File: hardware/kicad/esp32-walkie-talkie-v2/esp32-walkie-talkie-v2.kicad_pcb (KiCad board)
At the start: 2 copper layers, 68.6 x 53.3 mm, 22 parts, among them J1 inmp441 left, J2 inmp441 right, J3 ST7789, J4 extend, J5 POWER_IN_5V, J6 MAX98357, J7 POWER_IN_5V, P1 Power, P2 Analog, P3 Digital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

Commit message: update silk, export gerber
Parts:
- added kibuzzard-62A4A288: G***, kibuzzard-62A4A288, F.Cu at (130.0, 88.3)
- added kibuzzard-62A4A2A0: G***, kibuzzard-62A4A2A0, F.Cu at (122.9, 106.6)
- added kibuzzard-62A534F6: G***, kibuzzard-62A534F6, F.Cu at (171.7, 82.2)
- added kibuzzard-62A53545: G***, kibuzzard-62A53545, F.Cu at (114.3, 106.8)
- added kibuzzard-62A53555: G***, kibuzzard-62A53555, F.Cu at (130.0, 90.6)
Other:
- board text added: "LRC"
- board text removed: "LRCLK"

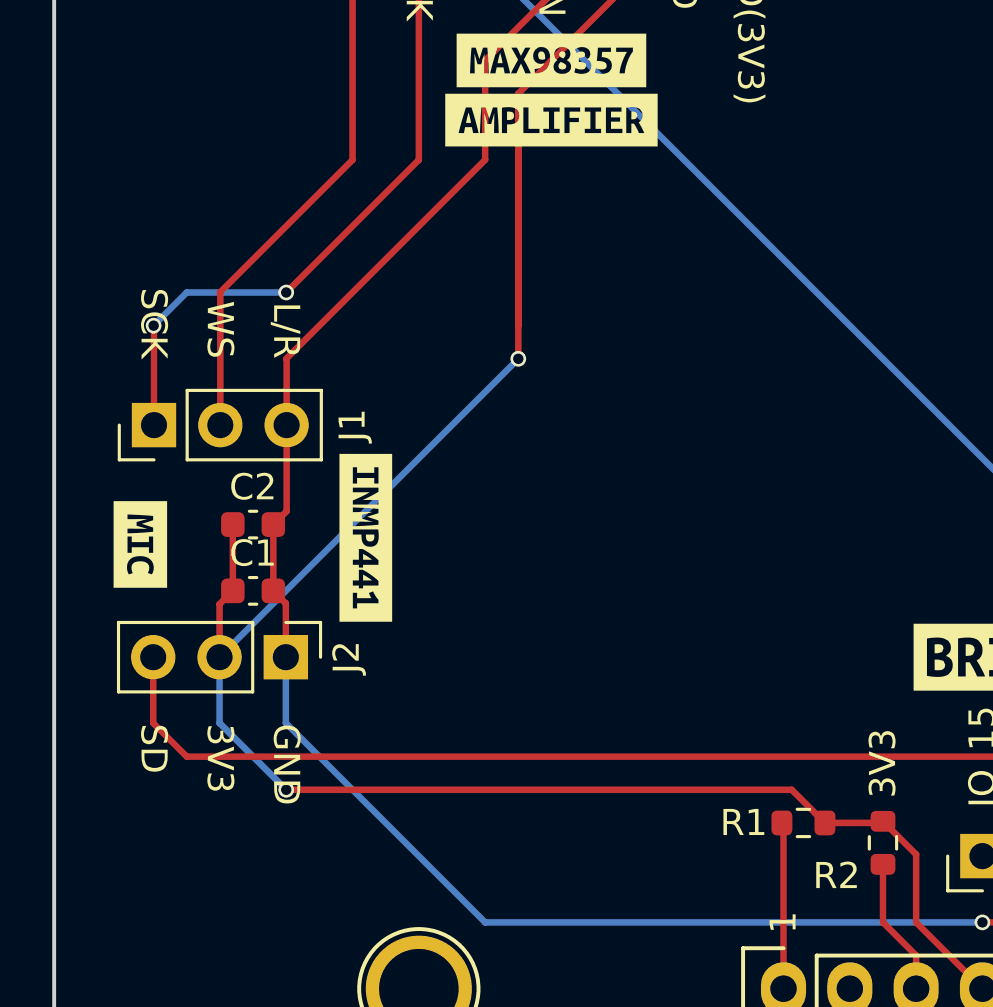
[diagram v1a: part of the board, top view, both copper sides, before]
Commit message: add option capacitor
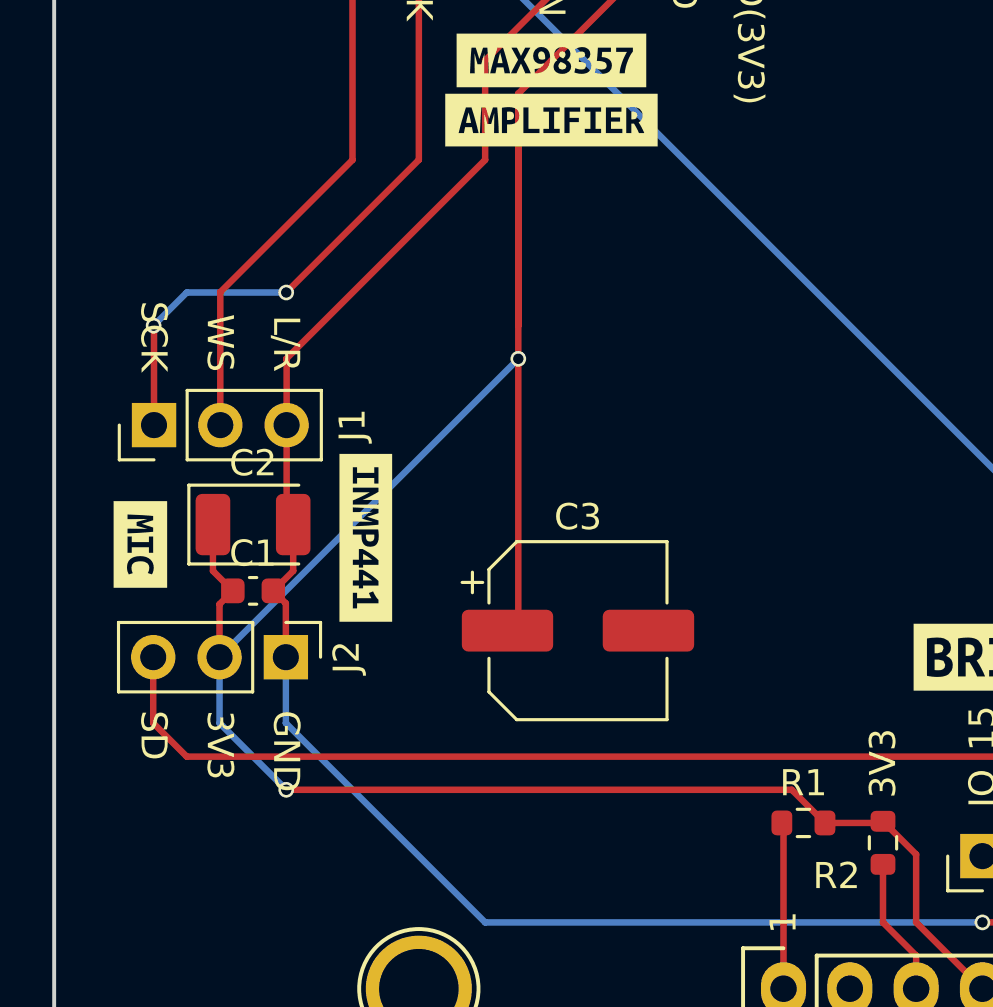
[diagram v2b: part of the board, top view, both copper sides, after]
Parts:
- added C3: 47uF, Capacitor_SMD:CP_Elec_6.3x5.8, F.Cu at (131.1, 110.1)
- C2: value 1uF -> 10uF; footprint Capacitor_SMD:C_0603_1608Metric -> Capacitor_Tantalum_SMD:CP_EIA-3528-12_Kemet-T
- J7: value POWER_IN_5V -> Transimit switch
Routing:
- net ESPDUINO_3.3V: track 142.5 -> 153.4 mm

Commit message: add rect capacitor option
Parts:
- added C4: 47uF, Capacitor_THT:C_Rect_L7.0mm_W2.0mm_P5.00mm, F.Cu at (128.6, 118.5)
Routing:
- net ESPDUINO_3.3V: track 153.4 -> 167.0 mm, vias 3 -> 4
- net GND: vias 1 -> 18
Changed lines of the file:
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@@
       ) (layer "F.SilkS") (width 0) (fill solid))
+  )
+  (footprint "Capacitor_THT:C_Rect_L7.0mm_W2.0mm_P5.00mm" (layer "F.Cu")
+    (at 128.564 118.491)
+    (descr "C, Rect series, Radial, pin pitch=5.00mm, , length*width=7*2mm^2, Capacitor")
+    (tags "C Rect series Radial pin pitch 5.00mm  length 7mm width 2mm Capacitor")
+    (property "Sheetfile" "esp32-walkie-talkie-v2.kicad_sch")
+    (property "Sheetname" "")
+    (attr through_hole)
+    (fp_text reference "C4" (at 2.5 -2.25) (layer "F.SilkS")
+      (effects (font (size 1 1) (thickness 0.15)))
+    )
+    (fp_text value "47uF" (at 2.5 2.25) (layer "F.Fab")
+      (effects (font (size 1 1) (thickness 0.15)))
+    )
+    (fp_text user "${REFERENCE}" (at 2.5 0) (layer "F.Fab")
+      (effects (font (size 1 1) (thickness 0.15)))
+    )
+    (fp_line (start -1.12 1.12) (end 6.12 1.12) (layer "F.SilkS") (width 0.12))
+    (fp_line (start 6.12 -1.12) (end 6.12 1.12) (layer "F.SilkS") (width 0.12))
+    (fp_line (start -1.12 -1.12) (end -1.12 1.12) (layer "F.SilkS") (width 0.12))
+    (fp_line (start -1.12 -1.12) (end 6.12 -1.12) (layer "F.SilkS") (width 0.12))
+    (fp_line (start 6.25 1.25) (end 6.25 -1.25) (layer "F.CrtYd") (width 0.05))
+    (fp_line (start 6.25 -1.25) (end -1.25 -1.25) (layer "F.CrtYd") (width 0.05))
+    (fp_line (start -1.25 -1.25) (end -1.25 1.25) (layer "F.CrtYd") (width 0.05))
+    (fp_line (start -1.25 1.25) (end 6.25 1.25) (layer "F.CrtYd") (width 0.05))
+    (fp_line (start 6 -1) (end -1 -1) (layer "F.Fab") (width 0.1))
+    (fp_line (start 6 1) (end 6 -1) (layer "F.Fab") (width 0.1))
+    (fp_line (start -1 1) (end 6 1) (layer "F.Fab") (width 0.1))
+    (fp_line (start -1 -1) (end -1 1) (layer "F.Fab") (width 0.1))
+    (pad "1" thru_hole circle (at 0 0) (size 1.6 1.6) (drill 0.8) (layers *.Cu *.Mask)
+      (net 34 "ESPDUINO_3.3V") (pintype "passive"))
+    (pad "2" thru_hole circle (at 5 0) (size 1.6 1.6) (drill 0.8) (layers *.Cu *.Mask)
+      (net 3 "GND") (pintype "passive"))
+    (model "${KICAD6_3DMODEL_DIR}/Capacitor_THT.3dshapes/C_Rect_L7.0mm_W2.0mm_P5.00mm.wrl"
+      (offset (xyz 0 0 0))
+      (scale (xyz 1 1 1))
+      (rotate (xyz 0 0 0))
+    )
   )
   (footprint "Capacitor_SMD:C_0603_1608Metric" (layer "F.Cu")
@@
   (segment (start 120.1555 107.8225) (end 119.393 108.585) (width 0.25) (layer "F.Cu") (net 3))
   (segment (start 119.903 99.71) (end 119.903 102.235) (width 0.25) (layer "F.Cu") (net 3))
+  (via (at 168.656 80.645) (size 0.6) (drill 0.4) (layers "F.Cu" "B.Cu") (free) (net 3))
+  (via (at 168.148 98.171) (size 0.6) (drill 0.4) (layers "F.Cu" "B.Cu") (free) (net 3))
+  (via (at 168.656 83.439) (size 0.6) (drill 0.4) (layers "F.Cu" "B.Cu") (free) (net 3))
+  (via (at 132.08 123.571) (size 0.6) (drill 0.4) (layers "F.Cu" "B.Cu") (free) (net 3))
+  (via (at 138.938 112.141) (size 0.6) (drill 0.4) (layers "F.Cu" "B.Cu") (free) (net 3))
   (via (at 146.558 121.285) (size 0.6) (drill 0.4) (layers "F.Cu" "B.Cu") (net 3))
+  (via (at 163.068 112.395) (size 0.6) (drill 0.4) (layers "F.Cu" "B.Cu") (free) (net 3))
+  (via (at 164.338 91.059) (size 0.6) (drill 0.4) (layers "F.Cu" "B.Cu") (free) (net 3))
+  (via (at 155.956 92.329) (size 0.6) (drill 0.4) (layers "F.Cu" "B.Cu") (free) (net 3))
+  (via (at 174.498 107.823) (size 0.6) (drill 0.4) (layers "F.Cu" "B.Cu") (free) (net 3))
+  (via (at 144.78 86.995) (size 0.6) (drill 0.4) (layers "F.Cu" "B.Cu") (free) (net 3))
+  (via (at 119.126 91.567) (size 0.6) (drill 0.4) (layers "F.Cu" "B.Cu") (free) (net 3))
+  (via (at 169.418 120.523) (size 0.6) (drill 0.4) (layers "F.Cu" "B.Cu") (free) (net 3))
+  (via (at 114.808 118.745) (size 0.6) (drill 0.4) (layers "F.Cu" "B.Cu") (free) (net 3))
+  (via (at 125.476 107.061) (size 0.6) (drill 0.4) (layers "F.Cu" "B.Cu") (free) (net 3))
+  (via (at 119.126 80.645) (size 0.6) (drill 0.4) (layers "F.Cu" "B.Cu") (free) (net 3))
+  (via (at 125.222 99.695) (size 0.6) (drill 0.4) (layers "F.Cu" "B.Cu") (free) (net 3))
+  (via (at 145.034 78.867) (size 0.6) (drill 0.4) (layers "F.Cu" "B.Cu") (free) (net 3))
   (segment (start 168.148 114.935) (end 170.688 114.935) (width 0.25) (layer "B.Cu") (net 3))
   (segment (start 155.448 121.285) (end 161.798 121.285) (width 0.25) (layer "B.Cu") (net 3))
@@
   (segment (start 117.0805 106.045) (end 117.0805 107.8225) (width 0.25) (layer "F.Cu") (net 34))
   (segment (start 142.685 117.475) (end 142.748 117.412) (width 0.25) (layer "F.Cu") (net 34))
+  (segment (start 124.714 112.141) (end 126.746 110.109) (width 0.25) (layer "F.Cu") (net 34))
   (segment (start 128.778 99.695) (end 128.778 109.695) (width 0.25) (layer "F.Cu") (net 34))
+  (segment (start 126.746 110.109) (end 128.364 110.109) (width 0.25) (layer "F.Cu") (net 34))
   (segment (start 128.778 109.695) (end 128.364 110.109) (width 0.25) (layer "F.Cu") (net 34))
   (segment (start 117.0805 107.8225) (end 117.843 108.585) (width 0.25) (layer "F.Cu") (net 34))
@@
   (segment (start 139.255 116.205) (end 119.888 116.205) (width 0.25) (layer "F.Cu") (net 34))
   (via (at 119.888 116.205) (size 0.6) (drill 0.4) (layers "F.Cu" "B.Cu") (net 34))
+  (via (at 124.714 112.141) (size 0.6) (drill 0.4) (layers "F.Cu" "B.Cu") (net 34))
   (via (at 168.148 94.615) (size 0.6) (drill 0.4) (layers "F.Cu" "B.Cu") (net 34))
   (via (at 128.778 99.695) (size 0.6) (drill 0.4) (layers "F.Cu" "B.Cu") (net 34))
@@
   (segment (start 117.333 113.65) (end 117.333 111.125) (width 0.25) (layer "B.Cu") (net 34))
   (segment (start 123.698 104.76) (end 123.713 104.76) (width 0.25) (layer "B.Cu") (net 34))
+  (segment (start 124.968 116.967) (end 124.714 116.713) (width 0.25) (layer "B.Cu") (net 34))
   (segment (start 174.498 90.85) (end 174.498 83.185) (width 0.25) (layer "B.Cu") (net 34))
   (segment (start 123.698 104.76) (end 117.333 111.125) (width 0.25) (layer "B.Cu") (net 34))
+  (segment (start 126.492 118.491) (end 124.968 116.967) (width 0.25) (layer "B.Cu") (net 34))
+  (segment (start 124.714 116.713) (end 124.714 112.141) (width 0.25) (layer "B.Cu") (net 34))
   (segment (start 123.713 104.76) (end 128.778 99.695) (width 0.25) (layer "B.Cu") (net 34))
+  (segment (start 128.564 118.491) (end 126.492 118.491) (width 0.25) (layer "B.Cu") (net 34))
   (segment (start 168.168 94.635) (end 168.148 94.615) (width 0.25) (layer "B.Cu") (net 34))
   (segment (start 170.713 94.635) (end 174.498 90.85) (width 0.25) (layer "B.Cu") (net 34))

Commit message: add text, new copper fill
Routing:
- net GND: track 105.4 -> 0.00 mm, vias 18 -> 17
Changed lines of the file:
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@@
     (fp_line (start -1.05 -1.4) (end -1.75 -0.7) (layer "F.Fab") (width 0.1))
     (fp_line (start 1.75 1.4) (end 1.75 -1.4) (layer "F.Fab") (width 0.1))
-    (pad "1" smd roundrect (at -1.5375 0) (size 1.325 2.35) (layers "F.Cu" "F.Paste" "F.Mask") (roundrect_rratio 0.188679)
+    (pad "1" smd roundrect (at -1.5375 0) (size 1.325 2.35) (layers "F.Cu" "F.Paste" "F.Mask") (roundrect_rratio 0.1886792453)
       (net 34 "ESPDUINO_3.3V") (pintype "passive"))
-    (pad "2" smd roundrect (at 1.5375 0) (size 1.325 2.35) (layers "F.Cu" "F.Paste" "F.Mask") (roundrect_rratio 0.188679)
+    (pad "2" smd roundrect (at 1.5375 0) (size 1.325 2.35) (layers "F.Cu" "F.Paste" "F.Mask") (roundrect_rratio 0.1886792453)
       (net 3 "GND") (pintype "passive"))
     (model "${KICAD6_3DMODEL_DIR}/Capacitor_Tantalum_SMD.3dshapes/CP_EIA-3528-12_Kemet-T.wrl"
@@
   (segment (start 138.875 117.475) (end 138.938 117.538) (width 0.25) (layer "F.Cu") (net 1))
   (segment (start 138.938 117.538) (end 138.938 123.825) (width 0.25) (layer "F.Cu") (net 1))
-  (segment (start 127.508 92.075) (end 119.888 99.695) (width 0.25) (layer "F.Cu") (net 3))
-  (segment (start 119.888 99.695) (end 119.903 99.71) (width 0.25) (layer "F.Cu") (net 3))
-  (segment (start 119.873 111.125) (end 119.873 109.065) (width 0.25) (layer "F.Cu") (net 3))
-  (segment (start 119.903 105.7925) (end 120.1555 106.045) (width 0.25) (layer "F.Cu") (net 3))
-  (segment (start 127.508 88.265) (end 127.508 92.075) (width 0.25) (layer "F.Cu") (net 3))
-  (segment (start 149.098 121.285) (end 146.558 121.285) (width 0.25) (layer "F.Cu") (net 3))
-  (segment (start 137.414 75.565) (end 137.414 77.089) (width 0.25) (layer "F.Cu") (net 3))
-  (segment (start 119.903 102.235) (end 119.903 105.7925) (width 0.25) (layer "F.Cu") (net 3))
-  (segment (start 135.128 80.645) (end 127.508 88.265) (width 0.25) (layer "F.Cu") (net 3))
-  (segment (start 151.638 123.825) (end 149.098 121.285) (width 0.25) (layer "F.Cu") (net 3))
-  (segment (start 120.1555 106.045) (end 120.1555 107.8225) (width 0.25) (layer "F.Cu") (net 3))
-  (segment (start 135.128 79.375) (end 135.128 80.645) (width 0.25) (layer "F.Cu") (net 3))
-  (segment (start 137.414 77.089) (end 135.128 79.375) (width 0.25) (layer "F.Cu") (net 3))
-  (segment (start 119.873 109.065) (end 119.393 108.585) (width 0.25) (layer "F.Cu") (net 3))
-  (segment (start 120.1555 107.8225) (end 119.393 108.585) (width 0.25) (layer "F.Cu") (net 3))
-  (segment (start 119.903 99.71) (end 119.903 102.235) (width 0.25) (layer "F.Cu") (net 3))
   (via (at 168.656 80.645) (size 0.6) (drill 0.4) (layers "F.Cu" "B.Cu") (free) (net 3))
   (via (at 168.148 98.171) (size 0.6) (drill 0.4) (layers "F.Cu" "B.Cu") (free) (net 3))
@@
   (via (at 132.08 123.571) (size 0.6) (drill 0.4) (layers "F.Cu" "B.Cu") (free) (net 3))
   (via (at 138.938 112.141) (size 0.6) (drill 0.4) (layers "F.Cu" "B.Cu") (free) (net 3))
-  (via (at 146.558 121.285) (size 0.6) (drill 0.4) (layers "F.Cu" "B.Cu") (net 3))
   (via (at 163.068 112.395) (size 0.6) (drill 0.4) (layers "F.Cu" "B.Cu") (free) (net 3))
   (via (at 164.338 91.059) (size 0.6) (drill 0.4) (layers "F.Cu" "B.Cu") (free) (net 3))
@@
   (via (at 125.222 99.695) (size 0.6) (drill 0.4) (layers "F.Cu" "B.Cu") (free) (net 3))
   (via (at 145.034 78.867) (size 0.6) (drill 0.4) (layers "F.Cu" "B.Cu") (free) (net 3))
-  (segment (start 168.148 114.935) (end 170.688 114.935) (width 0.25) (layer "B.Cu") (net 3))
-  (segment (start 155.448 121.285) (end 161.798 121.285) (width 0.25) (layer "B.Cu") (net 3))
-  (segment (start 151.638 123.825) (end 154.178 123.825) (width 0.25) (layer "B.Cu") (net 3))
-  (segment (start 154.178 123.825) (end 154.178 122.555) (width 0.25) (layer "B.Cu") (net 3))
-  (segment (start 119.873 113.65) (end 119.873 111.125) (width 0.25) (layer "B.Cu") (net 3))
-  (segment (start 146.558 121.285) (end 127.508 121.285) (width 0.25) (layer "B.Cu") (net 3))
-  (segment (start 154.178 122.555) (end 155.448 121.285) (width 0.25) (layer "B.Cu") (net 3))
-  (segment (start 161.798 121.285) (end 168.148 114.935) (width 0.25) (layer "B.Cu") (net 3))
-  (segment (start 127.508 121.285) (end 119.873 113.65) (width 0.25) (layer "B.Cu") (net 3))
   (segment (start 142.748 119.062) (end 142.748 121.285) (width 0.25) (layer "F.Cu") (net 5))
   (segment (start 144.018 122.555) (end 144.018 123.825) (width 0.25) (layer "F.Cu") (net 5))
@@
   (segment (start 170.713 94.635) (end 174.498 90.85) (width 0.25) (layer "B.Cu") (net 34))
   (segment (start 170.713 94.635) (end 168.168 94.635) (width 0.25) (layer "B.Cu") (net 34))
-  (zone (net 3) (net_name "GND") (layers F&B.Cu) (hatch edge 0.508)
+  (zone (net 3) (net_name "GND") (layers F&B.Cu) (name "GND") (hatch edge 0.508)
     (connect_pads (clearance 0.508))
     (min_thickness 0.254) (filled_areas_thickness no)
-    (fill yes (thermal_gap 0.508) (thermal_bridge_width 0.508))
+    (fill yes (mode hatch) (thermal_gap 0.508) (thermal_bridge_width 0.508) (smoothing chamfer) (island_removal_mode 2) (island_area_min 1)
+      (hatch_thickness 0.5) (hatch_gap 0.254) (hatch_orientation 0)
+      (hatch_smoothing_level 1) (hatch_smoothing_value 0.1)
+      (hatch_border_algorithm hatch_thickness) (hatch_min_hole_area 0.3))
     (polygon
       (pts
-        (xy 179.578 126.365)
-        (xy 110.998 126.365)
-        (xy 110.998 73.025)
-        (xy 179.578 73.025)
+        (xy 180.848 126.365)
+        (xy 110.744 126.365)
+        (xy 110.744 73.025)
+        (xy 180.848 73.025)
       )
     )
-  )
-  (zone (net 3) (net_name "GND") (layers F&B.Cu) (hatch edge 0.508)
-    (connect_pads (clearance 0.508))
-    (min_thickness 0.254) (filled_areas_thickness no)
-    (fill yes (thermal_gap 0.508) (thermal_bridge_width 0.508) (island_removal_mode 1) (island_area_min 0))
-    (polygon
-      (pts
-        (xy 179.578 126.365)
-        (xy 110.998 126.365)
-        (xy 110.998 73.025)
-        (xy 179.578 73.025)
-      )
-    )

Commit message: update
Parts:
- R1, R2: footprint Resistor_SMD:R_0603_1608Metric -> Resistor_SMD:R_1206_3216Metric
- moved R1 1.48 mm to (138.9, 118.7), turned to -90 degrees
- moved R2 0.57 mm to (143.0, 118.7)
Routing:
- net ESPDUINO_3.3V: track 167.0 -> 153.7 mm, vias 4 -> 3
- net ESPDUINO_IO0: track 6.38 -> 3.62 mm
- net ESPDUINO_IO19: track 48.3 -> 45.9 mm, vias 0 -> 1
- net RESET: track 5.29 -> 4.04 mm
